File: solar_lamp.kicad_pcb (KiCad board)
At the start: 2 copper layers, 68.1 x 68.1 mm, 11 parts, among them Q1 TP0604, SW1 DPDT, U1 MCP1700

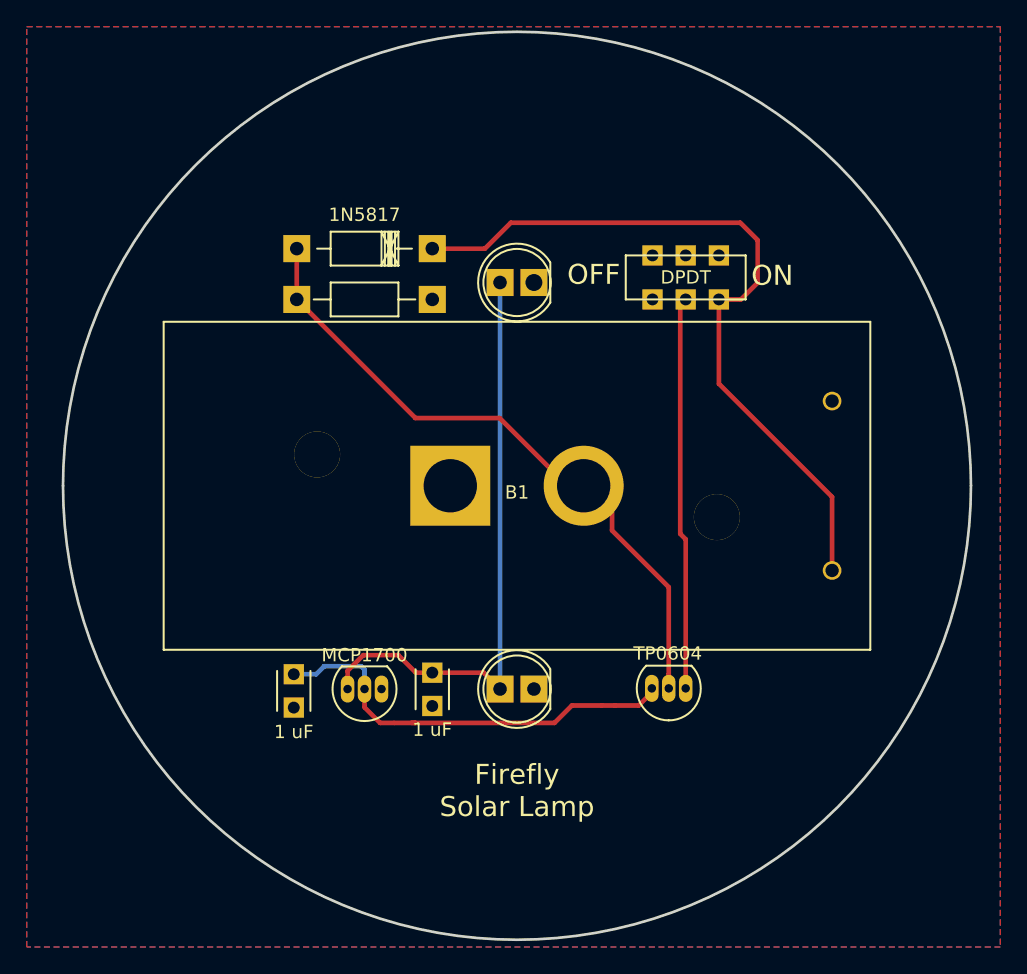
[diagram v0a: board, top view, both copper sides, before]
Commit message: chose transistor/ update footprints
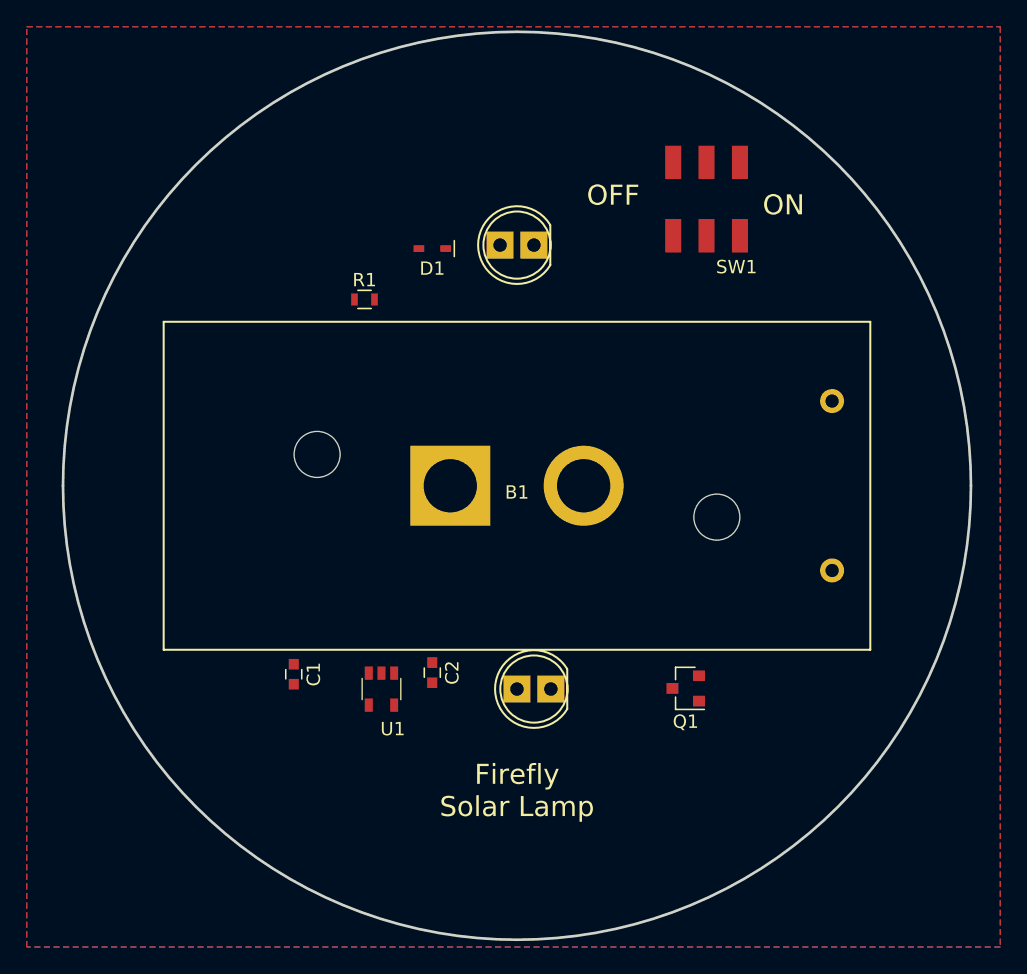
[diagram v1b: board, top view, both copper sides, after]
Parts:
- removed BT1: Solar Cell, firefly:Adafruit_round_solar_panel
- added SC1: Solar_Cell, solarlamp:Adafruit_round_solar_panel, B.Cu at (127.0, 127.0)
- B1: footprint firefly:Battery_Holder_Keystone_2468 -> solarlamp:Battery_Holder_Keystone_2468
- C1, C2: value 1 uF -> 1µ; footprint Capacitors_ThroughHole:C_Disc_D3_P2.5 -> Capacitors_SMD:C_0603
- D1: value 1N5817 -> D; footprint Diodes_ThroughHole:Diode_DO-41_SOD81_Horizontal_RM10 -> solarlamp:SOD-523F
- D2, D3: footprint LEDs:LED-5MM -> solarlamp:LED-5MM
- Q1: value TP0604 -> BSS84PH6327XTSA2; footprint TO_SOT_Packages_THT:TO-92_Inline_Narrow_Oval -> TO_SOT_Packages_SMD:SOT-23
- R1: footprint Resistors_ThroughHole:Resistor_Horizontal_RM10mm -> Resistors_SMD:R_0603
- SW1: value DPDT -> Switch_SPDT; footprint MikeMod:DPDT_JS202011CQN_switch -> solarlamp:DPDT_SMT
- U1: value MCP1700 -> BU21TD3WG; footprint TO_SOT_Packages_THT:TO-92_Inline_Narrow_Oval -> solarlamp:SSOP5
- moved SW1 6.08 mm to (141.2, 105.5)
- moved D3 3.08 mm to (127.0, 109.0)
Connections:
- D1 pad 2: Net-(BT1-Pad1) -> Net-(D1-Pad2)
- Q1 pad 1: Net-(Q1-Pad1) -> Net-(D1-Pad2)
- Q1 pad 2: Net-(BT1-Pad1) -> Net-(Q1-Pad2)
- R1 pad 1: Net-(BT1-Pad1) -> Net-(D1-Pad2)
- SW1 pad 1: (no net) -> Net-(Q1-Pad2)
- SW1 pad 2: (no net) -> Net-(B1-Pad1)
- SW1 pad 3: (no net) -> Net-(SW1-Pad3)
- U1 pad 1: GND -> Net-(C1-Pad1)
- U1 pad 2: Net-(C1-Pad1) -> GND
- U1 pad 3: Net-(C2-Pad1) -> Net-(C1-Pad1)
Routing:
- net Net-(B1-Pad1): track 56.2 -> 0.00 mm
- net Net-(BT1-Pad1): track 50.2 -> 0.00 mm
- net Net-(C2-Pad1): track 44.8 -> 0.00 mm
- net Net-(C1-Pad1): track 32.1 -> 0.00 mm
- net Net-(Q1-Pad1): track 28.9 -> 0.00 mm

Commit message: preliminary layout
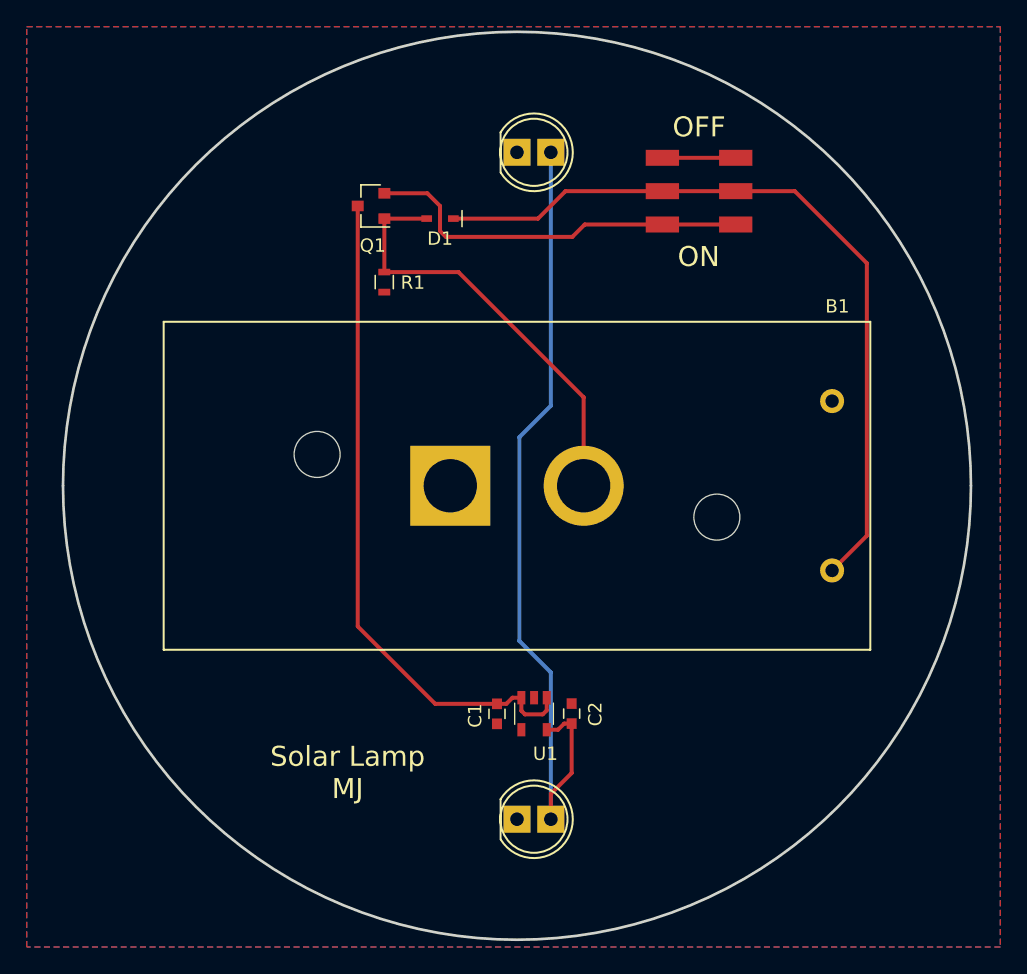
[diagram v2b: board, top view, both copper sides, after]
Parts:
- moved Q1 43.2 mm to (116.1, 106.0)
- moved C1 15.5 mm to (125.5, 144.1)
- moved U1 11.6 mm to (128.3, 144.1)
- moved C2 10.9 mm to (131.1, 144.1), turned to 90 degrees
- moved D2 9.76 mm to (128.3, 152.0), turned to 0 degrees
- moved D3 7.07 mm to (128.3, 102.0), turned to 0 degrees
- moved D1 2.32 mm to (121.2, 107.0)
- moved R1 1.97 mm to (117.0, 111.7), turned to 270 degrees
- moved SW1 0.82 mm to (140.7, 104.9), turned to 90 degrees
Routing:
- net Net-(C2-Pad1): track 0.00 -> 61.8 mm
- net Net-(B1-Pad1): track 0.00 -> 58.2 mm
- net Net-(C1-Pad1): track 0.00 -> 50.5 mm
- net Net-(D1-Pad2): track 0.00 -> 32.7 mm
- net Net-(Q1-Pad2): track 0.00 -> 29.2 mm
- net Net-(SW1-Pad3): track 0.00 -> 5.50 mm
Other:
- net class Default: clearance 0.25 -> 0.2; trace_width 0.35 -> 0.3; via_drill 0.4 -> 0.3
- rule pad_to_mask_clearance: 0.2 -> 0.1
- rule trace_clearance: 0.25 -> 0.2
- rule via_min_size: 0.4 -> 0.6
- board text added: "Solar Lamp MJ"
- board text removed: "Firefly Solar Lamp"

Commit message: changes in silkscreen
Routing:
- net Net-(C1-Pad1): track 50.5 -> 48.5 mm
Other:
- board text added: "Solar Lamp v2.0"
- board text removed: "Solar Lamp MJ"
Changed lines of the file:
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@@
     (links 22)
     (no_connects 0)
-    (area 92.863999 92.863999 161.136001 161.136001)
+    (area 90.24 92.58 163.240001 161.580001)
     (thickness 1.6)
     (drawings 5)
@@
     (tags "capacitor 0603")
     (attr smd)
-    (fp_text reference C1 (at 0.13 1.64 270) (layer F.SilkS)
+    (fp_text reference C1 (at 2.3 -0.02 540) (layer F.SilkS)
       (effects (font (size 1 1) (thickness 0.15)))
     )
@@
     (tags "capacitor 0603")
     (attr smd)
-    (fp_text reference C2 (at -0.04 1.77 270) (layer F.SilkS)
+    (fp_text reference C2 (at -2.32 0 180) (layer F.SilkS)
       (effects (font (size 1 1) (thickness 0.15)))
     )
@@
       (net 1 GND))
   )
+  (module solarlamp:SSOP5 (layer F.Cu)
+    (at 128.28 144.09 180)
+    (fp_text reference U1 (at 1.04 3 180) (layer F.SilkS)
+      (effects (font (size 1 1) (thickness 0.15)))
+    )
+    (fp_text value BU21TD3WG (at 0 3 180) (layer F.Fab) hide
+      (effects (font (size 1 1) (thickness 0.15)))
+    )
+    (fp_line (start 1.45 -0.8) (end 1.45 0.8) (layer F.SilkS) (width 0.15))
+    (fp_line (start -1.45 -0.8) (end -1.45 0.8) (layer F.SilkS) (width 0.15))
+    (pad 1 smd rect (at -0.95 1.2 180) (size 0.6 1) (layers F.Cu F.Paste F.Mask)
+      (net 2 "Net-(C1-Pad1)"))
+    (pad 2 smd rect (at 0 1.2 180) (size 0.6 1) (layers F.Cu F.Paste F.Mask)
+      (net 1 GND))
+    (pad 3 smd rect (at 0.95 1.2 180) (size 0.6 1) (layers F.Cu F.Paste F.Mask)
+      (net 2 "Net-(C1-Pad1)"))
+    (pad 4 smd rect (at 0.95 -1.2 180) (size 0.6 1) (layers F.Cu F.Paste F.Mask)
+      (net 8 "Net-(U1-Pad4)"))
+    (pad 5 smd rect (at -0.95 -1.2 180) (size 0.6 1) (layers F.Cu F.Paste F.Mask)
+      (net 3 "Net-(C2-Pad1)"))
+  )
   (module solarlamp:DPDT_SMT (layer F.Cu)
     (at 140.65 104.91 90)
-    (fp_text reference SW1 (at -2.25 -5.1 90) (layer F.SilkS) hide
+    (fp_text reference SW1 (at 5.1 -5.41 180) (layer F.SilkS)
       (effects (font (size 1 1) (thickness 0.15)))
     )
@@
       (effects (font (size 1 1) (thickness 0.15)))
     )
+    (fp_line (start -4.5 -2) (end -4.5 2) (layer F.SilkS) (width 0.15))
+    (fp_line (start 4.5 -2) (end 4.5 2) (layer F.SilkS) (width 0.15))
     (pad 1 smd trapezoid (at -2.5 2.75 90) (size 1.2 2.5) (layers F.Cu F.Paste F.Mask)
       (net 6 "Net-(Q1-Pad2)"))
@@
       (net 6 "Net-(Q1-Pad2)"))
   )
-  (module solarlamp:SSOP5 (layer F.Cu)
-    (at 128.28 144.09 180)
-    (fp_text reference U1 (at -0.85 -3 180) (layer F.SilkS)
-      (effects (font (size 1 1) (thickness 0.15)))
-    )
-    (fp_text value BU21TD3WG (at 0 3 180) (layer F.Fab) hide
-      (effects (font (size 1 1) (thickness 0.15)))
-    )
-    (fp_line (start 1.45 -0.8) (end 1.45 0.8) (layer F.SilkS) (width 0.05))
-    (fp_line (start -1.45 -0.8) (end -1.45 0.8) (layer F.SilkS) (width 0.05))
-    (pad 1 smd rect (at -0.95 1.2 180) (size 0.6 1) (layers F.Cu F.Paste F.Mask)
-      (net 2 "Net-(C1-Pad1)"))
-    (pad 2 smd rect (at 0 1.2 180) (size 0.6 1) (layers F.Cu F.Paste F.Mask)
-      (net 1 GND))
-    (pad 3 smd rect (at 0.95 1.2 180) (size 0.6 1) (layers F.Cu F.Paste F.Mask)
-      (net 2 "Net-(C1-Pad1)"))
-    (pad 4 smd rect (at 0.95 -1.2 180) (size 0.6 1) (layers F.Cu F.Paste F.Mask)
-      (net 8 "Net-(U1-Pad4)"))
-    (pad 5 smd rect (at -0.95 -1.2 180) (size 0.6 1) (layers F.Cu F.Paste F.Mask)
-      (net 3 "Net-(C2-Pad1)"))
-  )
   (module solarlamp:LED-5MM (layer F.Cu)
-    (at 128.27 102)
+    (at 128.27 152)
     (descr "LED 5mm round vertical")
     (tags "LED 5mm round vertical")
-    (fp_text reference D3 (at 0.254 4.064) (layer F.SilkS) hide
+    (fp_text reference D2 (at -0.1 4.67) (layer F.SilkS)
       (effects (font (size 1 1) (thickness 0.15)))
     )
@@
   )
   (module solarlamp:LED-5MM (layer F.Cu)
-    (at 128.27 152)
+    (at 128.27 102)
     (descr "LED 5mm round vertical")
     (tags "LED 5mm round vertical")
-    (fp_text reference D2 (at 0.254 4.064) (layer F.SilkS) hide
+    (fp_text reference D3 (at -0.05 -4.22) (layer F.SilkS)
       (effects (font (size 1 1) (thickness 0.15)))
     )
@@
     )
   )
-  (gr_text "Solar Lamp\nMJ" (at 114.3 148.51) (layer F.SilkS)
+  (gr_text "Solar Lamp\nv2.0" (at 114.41 147.33) (layer F.SilkS)
     (effects (font (size 1.5 1.5) (thickness 0.3)))
   )
   (gr_arc (start 127 127) (end 92.964 127) (angle 180) (layer Edge.Cuts) (width 0.2))
   (gr_arc (start 127 127) (end 161.036 127) (angle 180) (layer Edge.Cuts) (width 0.2))
-  (gr_text OFF (at 140.65 100.11) (layer F.SilkS)
+  (gr_text OFF (at 140.6 98.65) (layer F.SilkS)
     (effects (font (size 1.5 1.5) (thickness 0.3)))
   )
-  (gr_text ON (at 140.62 109.83) (layer F.SilkS)
+  (gr_text ON (at 140.59 111.19) (layer F.SilkS)
     (effects (font (size 1.5 1.5) (thickness 0.3)))
   )
@@
   (segment (start 126.66 142.89) (end 127.33 142.89) (width 0.3) (layer F.Cu) (net 2))
   (segment (start 126.2 143.35) (end 126.66 142.89) (width 0.3) (layer F.Cu) (net 2))
-  (segment (start 115.06 106.02) (end 115.06 137.54) (width 0.3) (layer F.Cu) (net 2))
-  (segment (start 120.87 143.35) (end 125.5 143.35) (width 0.3) (layer F.Cu) (net 2))
-  (segment (start 115.06 137.54) (end 120.87 143.35) (width 0.3) (layer F.Cu) (net 2))
+  (segment (start 115.06 106.02) (end 115.06 134.15) (width 0.3) (layer F.Cu) (net 2))
+  (segment (start 124.26 143.35) (end 125.5 143.35) (width 0.3) (layer F.Cu) (net 2))
+  (segment (start 115.06 134.15) (end 124.26 143.35) (width 0.3) (layer F.Cu) (net 2))
   (segment (start 129.54 102) (end 129.54 121) (width 0.3) (layer B.Cu) (net 3))
   (segment (start 129.54 141) (end 129.54 152) (width 0.3) (layer B.Cu) (net 3))

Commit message: repositioned diode
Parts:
- moved D1 39.5 mm to (141.2, 141.1)
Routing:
- net Net-(D1-Pad2): track 32.7 -> 49.2 mm
- net Net-(B1-Pad1): track 58.2 -> 56.0 mm
- net Net-(Q1-Pad2): track 29.2 -> 27.3 mm
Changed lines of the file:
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@@
     (links 22)
     (no_connects 0)
-    (area 90.24 92.58 163.240001 161.580001)
+    (area 92.863999 92.863999 161.136001 161.136001)
     (thickness 1.6)
     (drawings 5)
-    (tracks 45)
+    (tracks 47)
     (zones 0)
     (modules 11)
@@
   )
   (module solarlamp:SOD-523F (layer F.Cu)
-    (at 121.23 106.97 180)
+    (at 141.16 141.1 180)
     (descr "http://www.diodes.com/datasheets/ap02001.pdf p.144")
     (tags "Diode SOD523")
@@
   (segment (start 131.1 148.54) (end 131.1 144.83) (width 0.3) (layer F.Cu) (net 3))
   (segment (start 129.54 150.1) (end 131.1 148.54) (width 0.3) (layer F.Cu) (net 3))
+  (segment (start 142.16 141.1) (end 147.32 141.1) (width 0.3) (layer F.Cu) (net 4))
+  (segment (start 150.625 137.795) (end 150.625 133.35) (width 0.3) (layer F.Cu) (net 4))
+  (segment (start 147.32 141.1) (end 150.625 137.795) (width 0.3) (layer F.Cu) (net 4))
   (segment (start 143.4 104.91) (end 147.83 104.91) (width 0.3) (layer F.Cu) (net 4))
   (segment (start 153.23 130.745) (end 150.625 133.35) (width 0.3) (layer F.Cu) (net 4))
   (segment (start 153.23 110.31) (end 153.23 130.745) (width 0.3) (layer F.Cu) (net 4))
   (segment (start 147.83 104.91) (end 153.23 110.31) (width 0.3) (layer F.Cu) (net 4))
-  (segment (start 137.9 104.91) (end 130.64 104.91) (width 0.3) (layer F.Cu) (net 4))
-  (segment (start 128.58 106.97) (end 122.23 106.97) (width 0.3) (layer F.Cu) (net 4))
-  (segment (start 130.64 104.91) (end 128.58 106.97) (width 0.3) (layer F.Cu) (net 4))
   (segment (start 137.9 104.91) (end 143.4 104.91) (width 0.3) (layer F.Cu) (net 4))
+  (segment (start 132 127) (end 132 136.77) (width 0.3) (layer F.Cu) (net 5))
+  (segment (start 136.33 141.1) (end 140.16 141.1) (width 0.3) (layer F.Cu) (net 5))
+  (segment (start 132 136.77) (end 136.33 141.1) (width 0.3) (layer F.Cu) (net 5))
   (segment (start 132 127) (end 132 120.37) (width 0.3) (layer F.Cu) (net 5))
   (segment (start 122.61 110.98) (end 117.05 110.98) (width 0.3) (layer F.Cu) (net 5))
@@
   (segment (start 117.05 110.98) (end 117.06 110.97) (width 0.3) (layer F.Cu) (net 5))
   (segment (start 117.06 110.97) (end 117.06 106.97) (width 0.3) (layer F.Cu) (net 5))
-  (segment (start 117.06 106.97) (end 120.23 106.97) (width 0.3) (layer F.Cu) (net 5))
   (segment (start 117.06 105.07) (end 120.28 105.07) (width 0.3) (layer F.Cu) (net 6))
   (segment (start 132.08 107.41) (end 137.9 107.41) (width 0.3) (layer F.Cu) (net 6))
-  (segment (start 131.15 108.34) (end 132.08 107.41) (width 0.3) (layer F.Cu) (net 6))
-  (segment (start 121.67 108.34) (end 131.15 108.34) (width 0.3) (layer F.Cu) (net 6))
-  (segment (start 121.23 107.9) (end 121.67 108.34) (width 0.3) (layer F.Cu) (net 6))
-  (segment (start 121.23 106.02) (end 121.23 107.9) (width 0.3) (layer F.Cu) (net 6))
+  (segment (start 132.08 107.41) (end 132.08 107.41) (width 0.3) (layer F.Cu) (net 6))
+  (segment (start 122.61 107.41) (end 132.08 107.41) (width 0.3) (layer F.Cu) (net 6))
+  (segment (start 121.23 106.03) (end 122.61 107.41) (width 0.3) (layer F.Cu) (net 6))
+  (segment (start 121.23 106.02) (end 121.23 106.03) (width 0.3) (layer F.Cu) (net 6))
   (segment (start 120.28 105.07) (end 121.23 106.02) (width 0.3) (layer F.Cu) (net 6))
   (segment (start 137.9 107.41) (end 143.4 107.41) (width 0.3) (layer F.Cu) (net 6))

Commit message: add logo to silkscreen
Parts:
- added G***: LOGO, solarlamp:giraffe, F.Cu at (115.0, 147.6)
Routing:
- net Net-(B1-Pad1): track 56.0 -> 54.3 mm
- net Net-(D1-Pad2): track 49.2 -> 47.6 mm
